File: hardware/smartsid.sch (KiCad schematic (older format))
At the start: 35 parts, among them P1 INPUT, P2 CONTROL, P3 POT2, P4 SOCKET, P5 OUTPUT, U1 GAL16V8, U2 SID2, U3 7812, U4 7809, U5 SID1

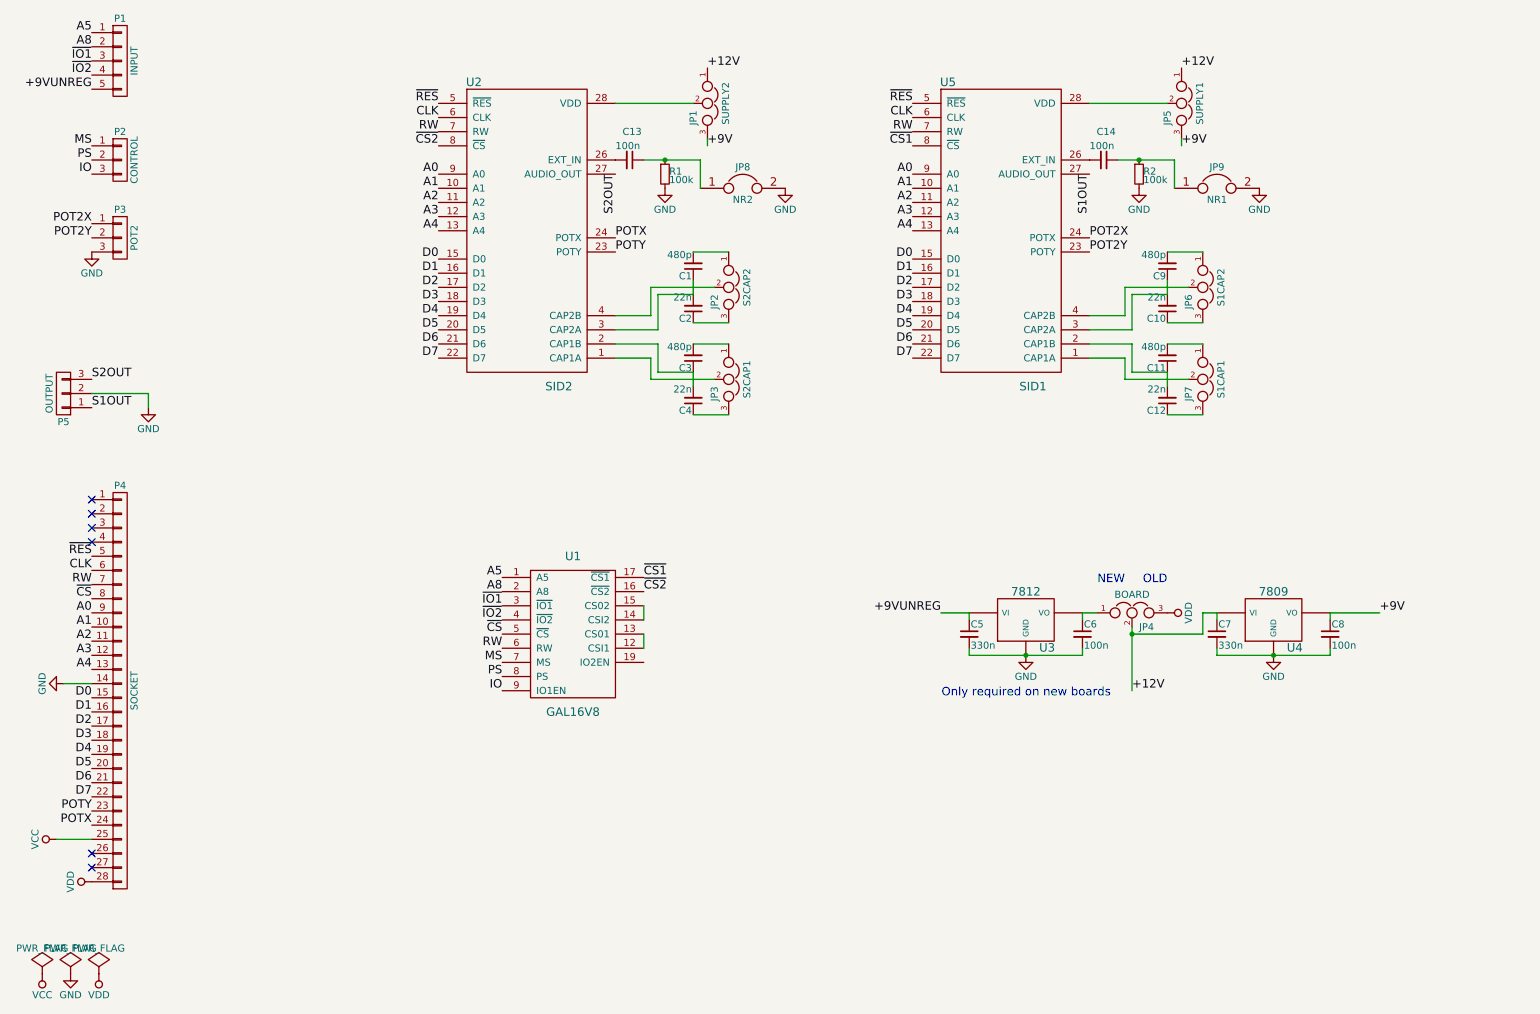
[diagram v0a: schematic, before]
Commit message: Hardware: Added mixing and simple opamp output circuit
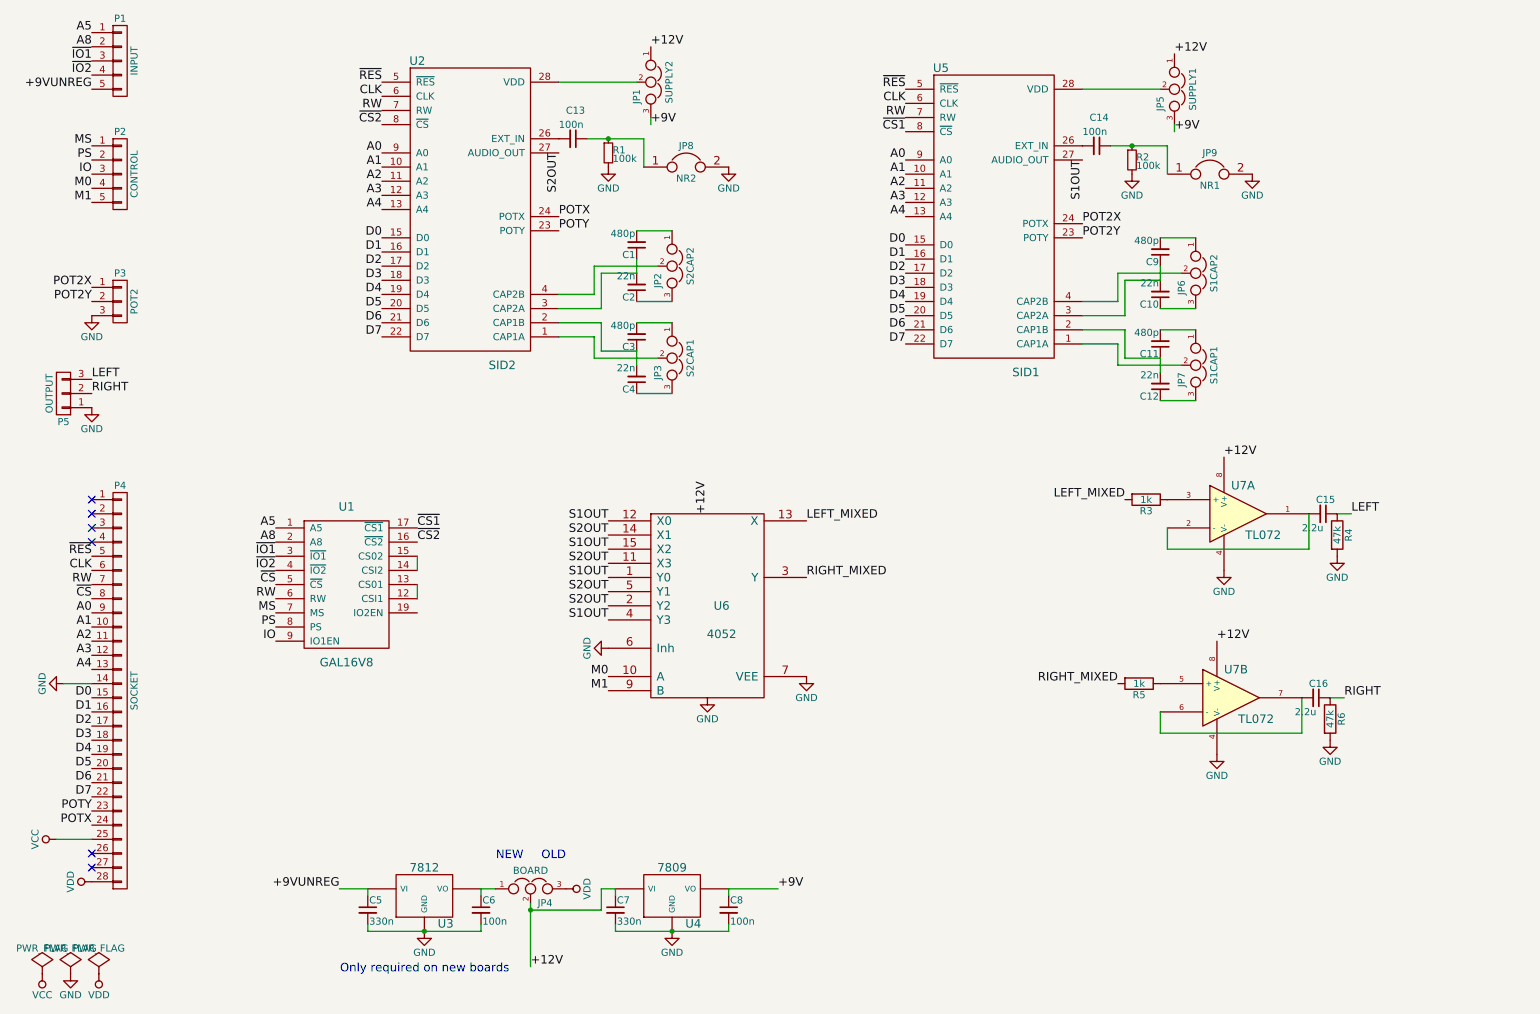
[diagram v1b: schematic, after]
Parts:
- removed P2: CONTROL, Pin_Headers:Pin_Header_Straight_1x03, symbol CONN_01X03
- added C15, C16: 2.2u, Capacitors_ThroughHole:C_Disc_D3_P2.5, symbol C_Small
- added P2: CONTROL, Pin_Headers:Pin_Header_Straight_1x05, symbol CONN_01X05
- added R3, R5: 1k, Discret:R1, symbol R
- added R4, R6: 47k, Discret:R1, symbol R
- added U6: 4052, Housings_DIP:DIP-16_W7.62mm, symbol 4052
- added U7: TL072, Housings_DIP:DIP-8_W7.62mm, symbol TL072
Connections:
- net +12V is gone; now on net VDD: C7.1, JP1.1, JP4.2, JP5.1, U4.1 (VI)
- net GND: now also P5.1 (P1), R4.2, R6.2, U6.6 (Inh), U6.7 (VEE), U6.8 (VSS), U7.4 (V-), U7.4 (V-); no longer P5.2 (P2)
- net IO: now also P2.3 (P3)
- net MS: now also P2.1 (P1)
- net PS: now also P2.2 (P2)
- net S1OUT: now also U6.1 (Y0), U6.12 (X0), U6.15 (X2), U6.4 (Y3); no longer P5.1 (P1)
- net S2OUT: now also U6.11 (X3), U6.14 (X1), U6.2 (Y2), U6.5 (Y1); no longer P5.3 (P3)
- net VDD: now also U6.16 (VDD), U7.8 (V+), U7.8 (V+)
- new net: R5.1, U7.5 (+)
- new net: C16.2, U7.6 (-), U7.7
- new net: C15.2, U7.1, U7.2 (-)
- new net: R3.1, U7.3 (+)
- new net LEFT: C15.1, P5.3 (P3), R4.1
- new net LEFT_MIXED: R3.2, U6.13 (X)
- new net M0: P2.4 (P4), U6.10 (A)
- new net M1: P2.5 (P5), U6.9 (B)
- new net RIGHT: C16.1, P5.2 (P2), R6.1
- new net RIGHT_MIXED: R5.2, U6.3 (Y)
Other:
- moved on the sheet: C1, C10, C11, C12, C13, C14, C2, C3, C4, C5, C6, C7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

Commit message: Hardware: Added notes about where to get +16v on 250469
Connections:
- net +9VUNREG renamed +16V
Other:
- note added: "Only required on 250469"
- note added: "from positive \nlead of C66\non 250469"
- note removed: "Only required on new boards"
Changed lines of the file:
@@
 $EndComp
 Text Label 2800 6950 2    60   ~ 0
-+9VUNREG
++16V
 $Comp
 L C_Small C7
@@
 	1    0    0    -1
 $EndComp
-Text Label 1050 1300 2    60   ~ 0
-+9VUNREG
 $Comp
 L CONN_01X28 P4
@@
 Text Label 1050 2100 2    60   ~ 0
 M1
-Text Notes 4000 7550 2    60   ~ 0
-Only required on new boards
+Text Notes 3700 7600 2    60   ~ 0
+Only required on 250469
+Text Notes 2200 7250 0    60   ~ 0
+from positive \nlead of C66\non 250469
+Text Label 1050 1300 2    60   ~ 0
++16V
 $EndSCHEMATC

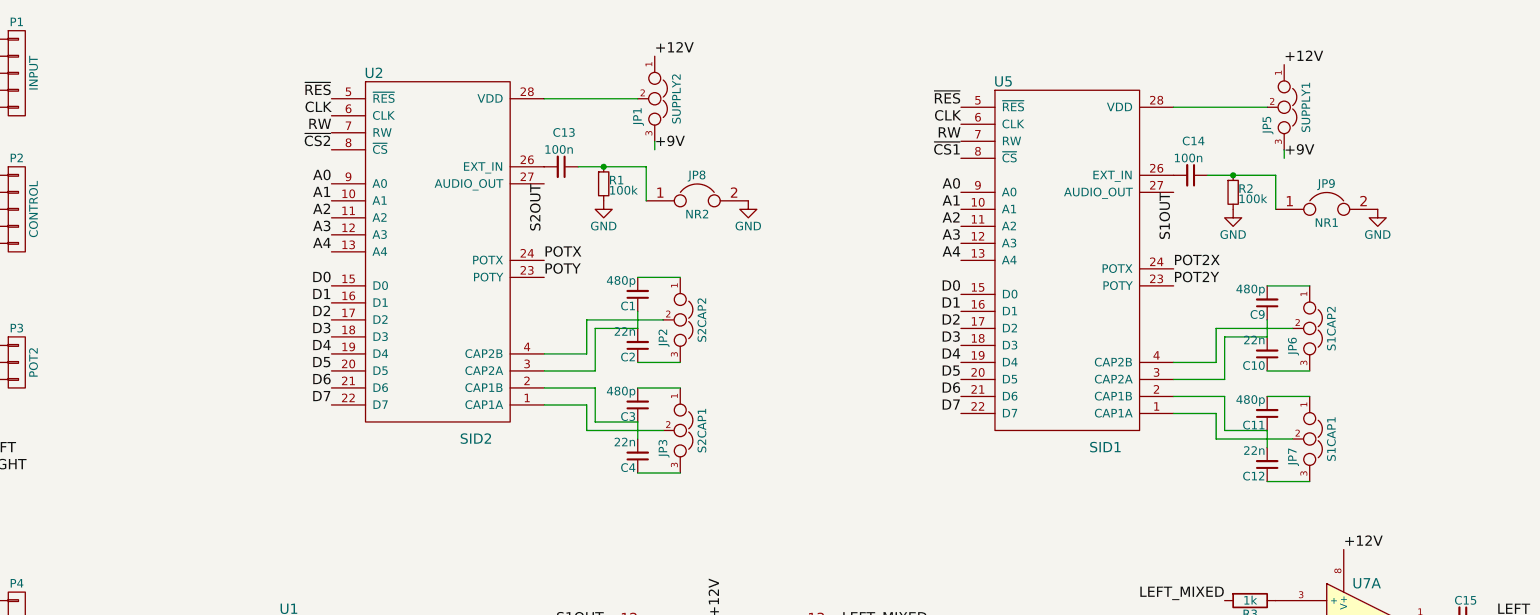
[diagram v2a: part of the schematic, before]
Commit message: Hardware: Added optional digifix circuits for both chips
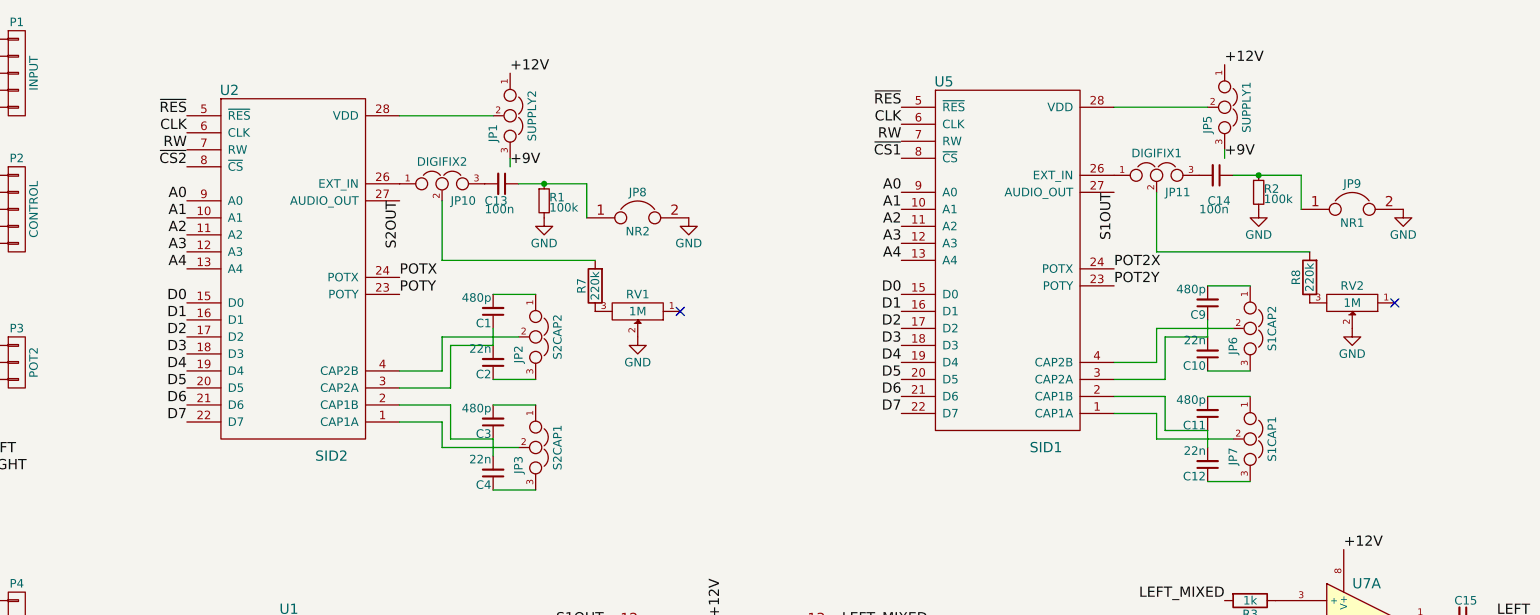
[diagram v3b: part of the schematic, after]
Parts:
- added JP10: DIGIFIX2, Pin_Headers:Pin_Header_Straight_1x03, symbol JUMPER3
- added JP11: DIGIFIX1, Pin_Headers:Pin_Header_Straight_1x03, symbol JUMPER3
- added R7, R8: 220k, Discret:R1, symbol R
- added RV1, RV2: 1M, Potentiometers:Potentiometer_Bourns_3339H_Angular_ScrewUp, symbol POT
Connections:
- net GND: now also RV1.2, RV2.2
- net at U5.26 (EXT_IN): now also JP11.1; no longer C14.2
- net at U2.26 (EXT_IN): now also JP10.1; no longer C13.2
- new net: C14.2, JP11.3
- new net: C13.2, JP10.3
- new net: R7.1, RV1.3
- new net: R8.1, RV2.3
- new net: JP11.2, R8.2
- new net: JP10.2, R7.2
- no-connect marks 6 -> 8
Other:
- moved on the sheet: C1, C10, C11, C12, C13, C14, C2, C3, C4, C9, JP1, JP2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
